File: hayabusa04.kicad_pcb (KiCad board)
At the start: 2 copper layers, 81.8 x 38.1 mm, 20 parts, among them SW1 SW_Push, SW2 MX_SW_HS, SW3 MX_SW_HS, SW4 MX_SW_HS, SW5 MX_SW_HS, U1 ATmega32U4-AU, Y1 16MHz

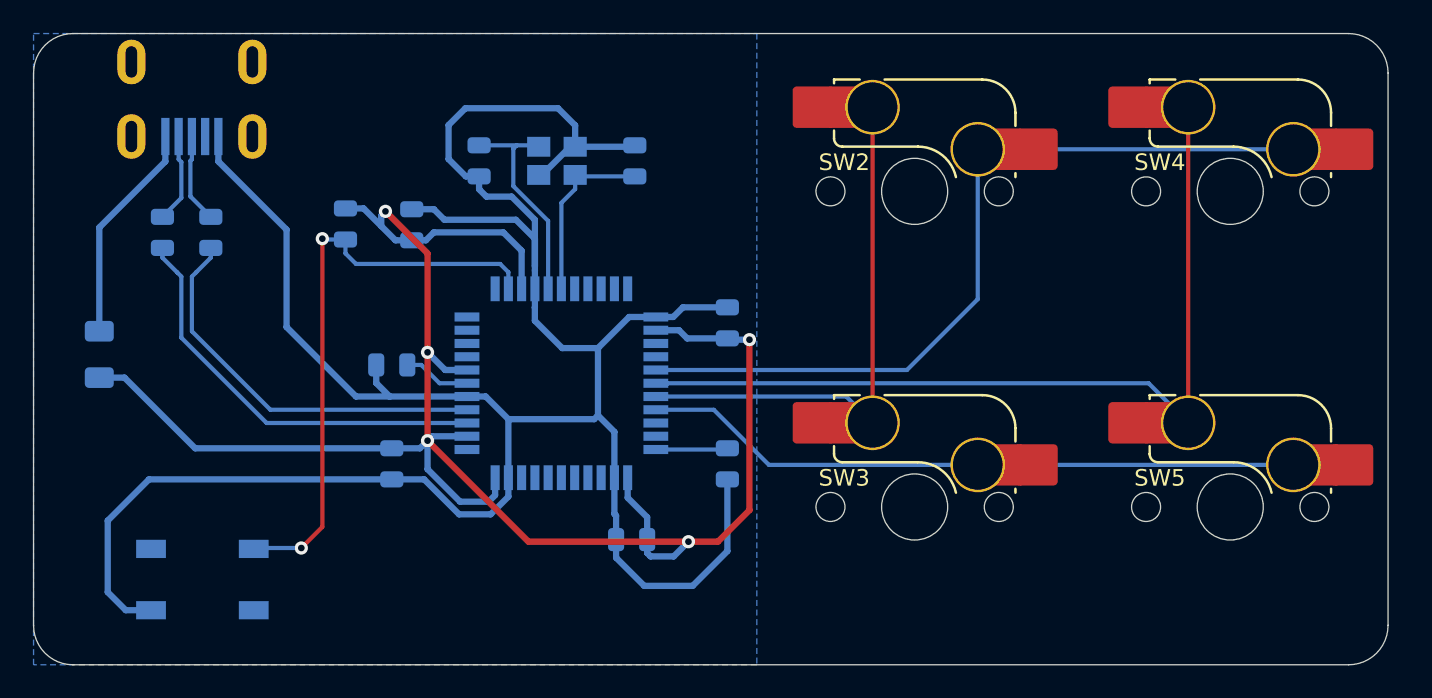
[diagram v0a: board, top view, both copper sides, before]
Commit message: routed usb c
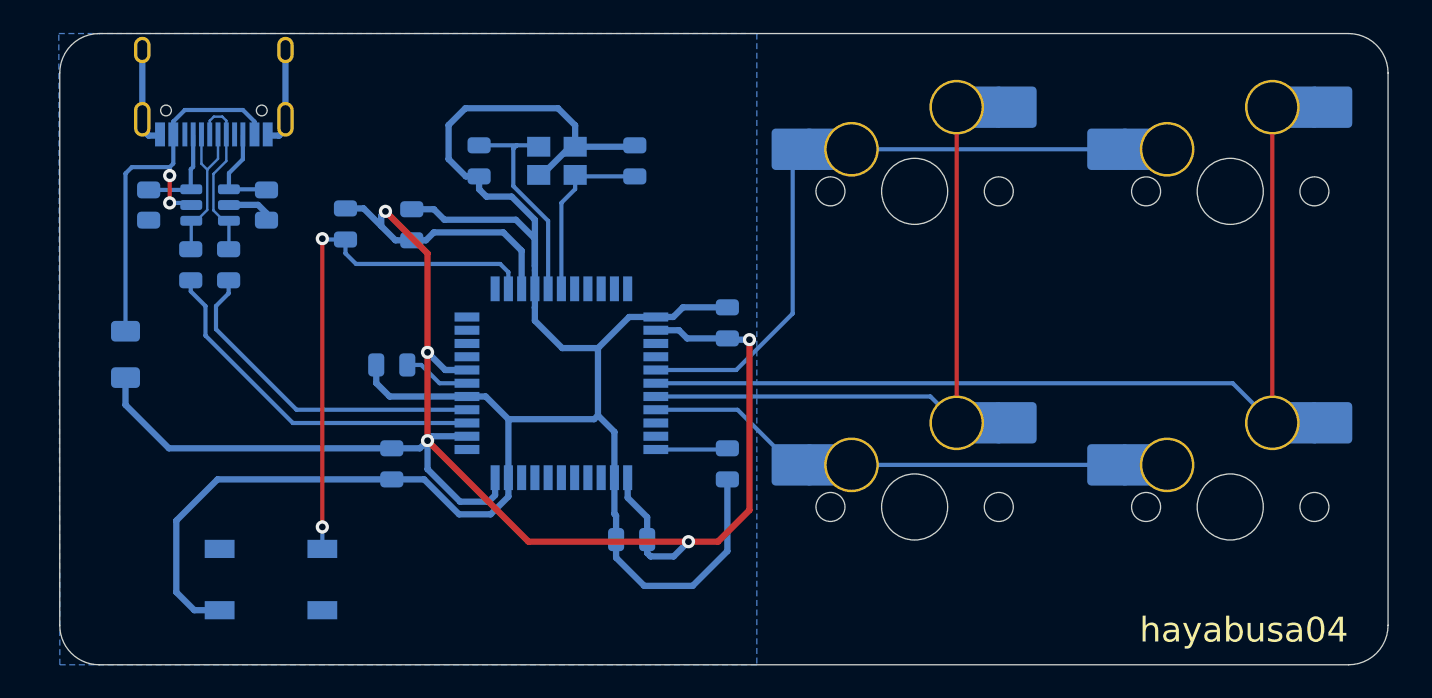
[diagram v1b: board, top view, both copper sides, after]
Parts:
- removed USB1: Molex-0548190589, random-keyboard-parts:Molex-0548190589
- added J1: USB_C_Receptacle_USB2.0, Connector_USB:USB_C_Receptacle_HRO_TYPE-C-31-M-12, B.Cu at (121.2, 57.6)
- added R5: 5.1k, Resistor_SMD:R_0805_2012Metric, B.Cu at (117.3, 65.9)
- added R6: 5.1k, Resistor_SMD:R_0805_2012Metric, B.Cu at (124.4, 65.9)
- added U2: SRV05-4, Package_TO_SOT_SMD:SOT-23-6, B.Cu at (121.0, 65.9)
- SW2, SW3, SW4, SW5: moved to B.Cu
- moved SW1 4.14 mm to (124.7, 88.5)
- moved R1 2.60 mm to (119.8, 69.5)
- moved R2 2.23 mm to (122.1, 69.5)
- moved F1 1.58 mm to (115.9, 74.9), turned to -90 degrees
- turned SW2 to 180 degrees
- turned SW3 to 180 degrees
- turned SW4 to 180 degrees
- turned SW5 to 180 degrees
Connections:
- F1 pad 1: +5V -> ESD5V
- F1 pad 2: VCC -> +5V
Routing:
- net ESD5V: track 0.00 -> 25.0 mm, vias 0 -> 2
- net ROW0: track 52.8 -> 38.6 mm
- net VCC: track 13.4 -> 0.00 mm
- net ROW1: track 39.9 -> 28.7 mm
- net GND: track 155.7 -> 145.3 mm
- net CC1: track 0.00 -> 5.92 mm
- net CC2: track 0.00 -> 5.89 mm
- net D+: track 5.40 -> 10.7 mm
- net COL0: track 32.8 -> 37.9 mm
- net D-: track 5.39 -> 9.96 mm
- net COL1: track 52.9 -> 57.2 mm
- net Net-(R2-Pad2): track 24.1 -> 20.4 mm
- net Net-(R1-Pad1): track 25.3 -> 21.7 mm
- net Net-(R3-Pad2): track 35.6 -> 32.3 mm
- net +5V: track 112.1 -> 111.5 mm
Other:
- board size 81.8 x 38.1 mm -> 80.2 x 38.1 mm
- board text added: "hayabusa04"

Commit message: generated gerber files
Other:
- rule pad_to_mask_clearance: 0.051 -> 0
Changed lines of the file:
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@@
   )
   (setup
-    (pad_to_mask_clearance 0.051)
-    (solder_mask_min_width 0.25)
+    (stackup
+      (layer "F.SilkS" (type "Top Silk Screen"))
+      (layer "F.Paste" (type "Top Solder Paste"))
+      (layer "F.Mask" (type "Top Solder Mask") (thickness 0.01))
+      (layer "F.Cu" (type "copper") (thickness 0.035))
+      (layer "dielectric 1" (type "core") (thickness 1.51) (material "FR4") (epsilon_r 4.5) (loss_tangent 0.02))
+      (layer "B.Cu" (type "copper") (thickness 0.035))
+      (layer "B.Mask" (type "Bottom Solder Mask") (thickness 0.01))
+      (layer "B.Paste" (type "Bottom Solder Paste"))
+      (layer "B.SilkS" (type "Bottom Silk Screen"))
+      (copper_finish "None")
+      (dielectric_constraints no)
+    )
+    (pad_to_mask_clearance 0)
     (pcbplotparams
-      (layerselection 0x00010fc_ffffffff)
+      (layerselection 0x00010f0_ffffffff)
       (disableapertmacros false)
-      (usegerberextensions false)
+      (usegerberextensions true)
       (usegerberattributes false)
       (usegerberadvancedattributes false)
@@
       (plotinvisibletext false)
       (sketchpadsonfab false)
-      (subtractmaskfromsilk false)
+      (subtractmaskfromsilk true)
       (outputformat 1)
       (mirror false)
-      (drillshape 1)
+      (drillshape 0)
       (scaleselection 1)
-      (outputdirectory "")
+      (outputdirectory "gerber/")
     )
   )
@@
     (fp_arc (start -4.864824 3.20022) (mid -4.718377 2.846667) (end -4.364824 2.70022) (layer "B.SilkS") (width 0.15))
     (fp_arc (start 2.494322 0.86022) (mid 1.670693 2.183637) (end 0.2 2.70022) (layer "B.SilkS") (width 0.15))
-    (fp_arc (start 6.085176 4.75022) (mid 5.499393 6.164439) (end 4.085176 6.75022) (layer "B.SilkS") (width 0.15))
+    (fp_arc (start 6.085176 4.75022) (mid 5.499394 6.164438) (end 4.085176 6.75022) (layer "B.SilkS") (width 0.15))
     (fp_line (start 9.525 9.525) (end 9.525 -9.525) (layer "Dwgs.User") (width 0.12))
     (fp_line (start 9.525 -9.525) (end -9.525 -9.525) (layer "Dwgs.User") (width 0.12))
@@
     (fp_line (start 8.685176 3.75022) (end 8.685176 1.30022) (layer "B.CrtYd") (width 0.05))
     (fp_arc (start 2.494322 0.86022) (mid 1.670502 2.183399) (end 0.2 2.70022) (layer "B.CrtYd") (width 0.05))
-    (fp_arc (start 6.085176 4.75022) (mid 5.499393 6.164439) (end 4.085176 6.75022) (layer "B.CrtYd") (width 0.05))
+    (fp_arc (start 6.085176 4.75022) (mid 5.499394 6.164438) (end 4.085176 6.75022) (layer "B.CrtYd") (width 0.05))
     (fp_line (start 7 7) (end 7 -7) (layer "F.CrtYd") (width 0.05))
     (fp_line (start -7 -7) (end -7 7) (layer "F.CrtYd") (width 0.05))
@@
     (fp_line (start -4.864824 6.75022) (end -4.864824 6.52022) (layer "B.SilkS") (width 0.15))
     (fp_line (start 4.085176 6.75022) (end -1.814824 6.75022) (layer "B.SilkS") (width 0.15))
-    (fp_arc (start 6.085176 4.75022) (mid 5.499393 6.164439) (end 4.085176 6.75022) (layer "B.SilkS") (width 0.15))
+    (fp_arc (start 6.085176 4.75022) (mid 5.499394 6.164438) (end 4.085176 6.75022) (layer "B.SilkS") (width 0.15))
     (fp_arc (start -4.864824 3.20022) (mid -4.718377 2.846667) (end -4.364824 2.70022) (layer "B.SilkS") (width 0.15))
     (fp_arc (start 2.494322 0.86022) (mid 1.670693 2.183637) (end 0.2 2.70022) (layer "B.SilkS") (width 0.15))
@@
     (fp_line (start 6.085176 3.75022) (end 8.685176 3.75022) (layer "B.CrtYd") (width 0.05))
     (fp_line (start -4.864824 2.70022) (end 0.2 2.70022) (layer "B.CrtYd") (width 0.05))
-    (fp_arc (start 6.085176 4.75022) (mid 5.499393 6.164439) (end 4.085176 6.75022) (layer "B.CrtYd") (width 0.05))
+    (fp_arc (start 6.085176 4.75022) (mid 5.499394 6.164438) (end 4.085176 6.75022) (layer "B.CrtYd") (width 0.05))
     (fp_arc (start 2.494322 0.86022) (mid 1.670502 2.183399) (end 0.2 2.70022) (layer "B.CrtYd") (width 0.05))
     (fp_line (start 7 7) (end 7 -7) (layer "F.CrtYd") (width 0.05))
@@
     (fp_line (start -1 -0.625) (end -1 0.625) (layer "B.Fab") (width 0.1))
     (fp_line (start -1 0.625) (end 1 0.625) (layer "B.Fab") (width 0.1))
-    (pad "1" smd roundrect (at -0.9125 0 270) (size 1.025 1.4) (layers "B.Cu" "B.Paste" "B.Mask") (roundrect_rratio 0.243902)
+    (pad "1" smd roundrect (at -0.9125 0 270) (size 1.025 1.4) (layers "B.Cu" "B.Paste" "B.Mask") (roundrect_rratio 0.243902439)
       (net 42 "CC2") (pintype "passive"))
-    (pad "2" smd roundrect (at 0.9125 0 270) (size 1.025 1.4) (layers "B.Cu" "B.Paste" "B.Mask") (roundrect_rratio 0.243902)
+    (pad "2" smd roundrect (at 0.9125 0 270) (size 1.025 1.4) (layers "B.Cu" "B.Paste" "B.Mask") (roundrect_rratio 0.243902439)
       (net 1 "GND") (pintype "passive"))
     (model "${KICAD6_3DMODEL_DIR}/Resistor_SMD.3dshapes/R_0805_2012Metric.wrl"
@@
     (fp_arc (start 2.494322 0.86022) (mid 1.670693 2.183637) (end 0.2 2.70022) (layer "B.SilkS") (width 0.15))
     (fp_arc (start -4.864824 3.20022) (mid -4.718377 2.846667) (end -4.364824 2.70022) (layer "B.SilkS") (width 0.15))
-    (fp_arc (start 6.085176 4.75022) (mid 5.499393 6.164439) (end 4.085176 6.75022) (layer "B.SilkS") (width 0.15))
+    (fp_arc (start 6.085176 4.75022) (mid 5.499394 6.164438) (end 4.085176 6.75022) (layer "B.SilkS") (width 0.15))
     (fp_line (start -9.525 -9.525) (end -9.525 9.525) (layer "Dwgs.User") (width 0.12))
     (fp_line (start -9.525 9.525) (end 9.525 9.525) (layer "Dwgs.User") (width 0.12))
@@
     (fp_line (start -7.414824 3.87022) (end -7.414824 6.32022) (layer "B.CrtYd") (width 0.05))
     (fp_line (start -4.864824 3.87022) (end -7.414824 3.87022) (layer "B.CrtYd") (width 0.05))
-    (fp_arc (start 6.085176 4.75022) (mid 5.499393 6.164439) (end 4.085176 6.75022) (layer "B.CrtYd") (width 0.05))
+    (fp_arc (start 6.085176 4.75022) (mid 5.499394 6.164438) (end 4.085176 6.75022) (layer "B.CrtYd") (width 0.05))
     (fp_arc (start 2.494322 0.86022) (mid 1.670502 2.183399) (end 0.2 2.70022) (layer "B.CrtYd") (width 0.05))
     (fp_line (start -7 -7) (end -7 7) (layer "F.CrtYd") (width 0.05))
@@
     (fp_line (start -1 -0.625) (end -1 0.625) (layer "B.Fab") (width 0.1))
     (fp_line (start -1 0.625) (end 1 0.625) (layer "B.Fab") (width 0.1))
-    (pad "1" smd roundrect (at -0.9125 0 90) (size 1.025 1.4) (layers "B.Cu" "B.Paste" "B.Mask") (roundrect_rratio 0.243902)
+    (pad "1" smd roundrect (at -0.9125 0 90) (size 1.025 1.4) (layers "B.Cu" "B.Paste" "B.Mask") (roundrect_rratio 0.243902439)
       (net 1 "GND") (pintype "passive"))
-    (pad "2" smd roundrect (at 0.9125 0 90) (size 1.025 1.4) (layers "B.Cu" "B.Paste" "B.Mask") (roundrect_rratio 0.243902)
+    (pad "2" smd roundrect (at 0.9125 0 90) (size 1.025 1.4) (layers "B.Cu" "B.Paste" "B.Mask") (roundrect_rratio 0.243902439)
       (net 41 "CC1") (pintype "passive"))
     (model "${KICAD6_3DMODEL_DIR}/Resistor_SMD.3dshapes/R_0805_2012Metric.wrl"
@@
     (fp_line (start -4.864824 6.75022) (end -4.864824 6.52022) (layer "B.SilkS") (width 0.15))
     (fp_arc (start -4.864824 3.20022) (mid -4.718377 2.846667) (end -4.364824 2.70022) (layer "B.SilkS") (width 0.15))
-    (fp_arc (start 6.085176 4.75022) (mid 5.499393 6.164439) (end 4.085176 6.75022) (layer "B.SilkS") (width 0.15))
+    (fp_arc (start 6.085176 4.75022) (mid 5.499394 6.164438) (end 4.085176 6.75022) (layer "B.SilkS") (width 0.15))
     (fp_arc (start 2.494322 0.86022) (mid 1.670693 2.183637) (end 0.2 2.70022) (layer "B.SilkS") (width 0.15))
     (fp_line (start -9.525 9.525) (end 9.525 9.525) (layer "Dwgs.User") (width 0.12))
@@
     (fp_line (start 6.085176 1.30022) (end 6.085176 0.86022) (layer "B.CrtYd") (width 0.05))
     (fp_arc (start 2.494322 0.86022) (mid 1.670502 2.183399) (end 0.2 2.70022) (layer "B.CrtYd") (width 0.05))
-    (fp_arc (start 6.085176 4.75022) (mid 5.499393 6.164439) (end 4.085176 6.75022) (layer "B.CrtYd") (width 0.05))
+    (fp_arc (start 6.085176 4.75022) (mid 5.499394 6.164438) (end 4.085176 6.75022) (layer "B.CrtYd") (width 0.05))
     (fp_line (start 7 -7) (end -7 -7) (layer "F.CrtYd") (width 0.05))
     (fp_line (start 7 7) (end 7 -7) (layer "F.CrtYd") (width 0.05))

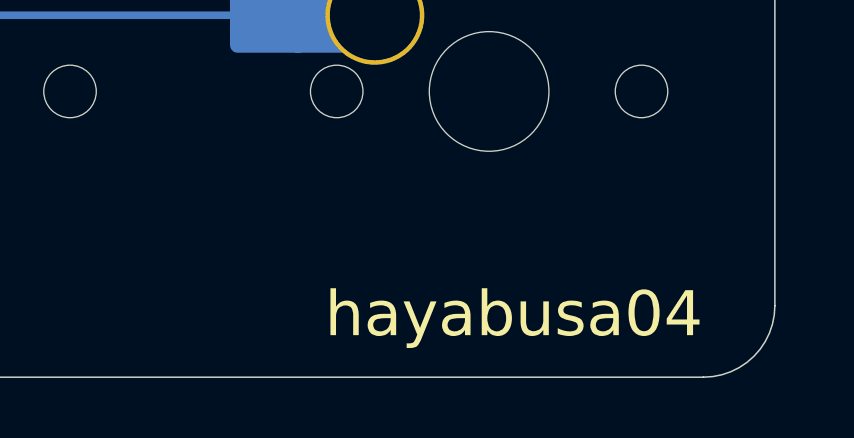
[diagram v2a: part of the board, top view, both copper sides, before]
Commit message: added 3d models
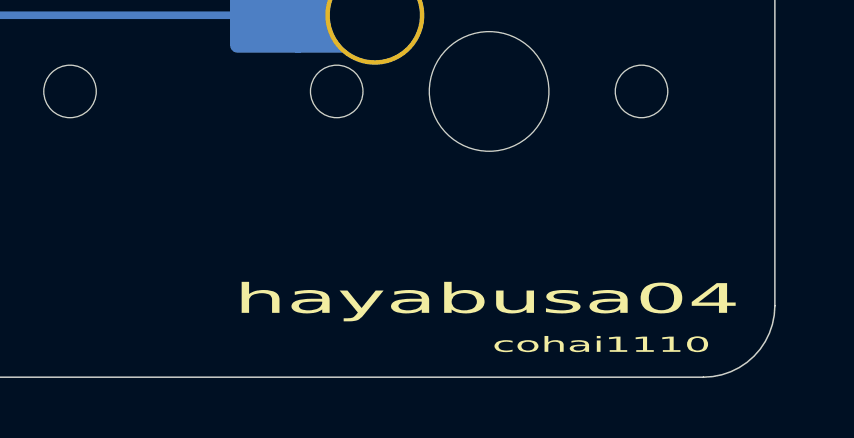
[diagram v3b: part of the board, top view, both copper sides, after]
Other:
- board text added: "cohai1110"
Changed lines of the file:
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@@
     (pad "3" smd rect locked (at 3.1 1.85 180) (size 1.8 1.1) (layers "B.Cu" "B.Paste" "B.Mask"))
     (pad "4" smd rect locked (at -3.1 -1.85 180) (size 1.8 1.1) (layers "B.Cu" "B.Paste" "B.Mask"))
-    (model "${KISYS3DMOD}/Button_Switch_SMD.3dshapes/SW_SPST_TL3342.step"
+    (model "${KICAD6_3DMODEL_DIR}/Button_Switch_SMD.3dshapes/SW_SPST_TL3342.step"
       (offset (xyz 0 0 0))
       (scale (xyz 1 1 1))
@@
       (rotate (xyz 180 0 0))
     )
+    (model "${KIPRJMOD}/marbastlib-mx.pretty/3d/HS_Kailh_MX.step"
+      (offset (xyz -4.826 6.7399916 1.905))
+      (scale (xyz 1 1 1))
+      (rotate (xyz 180 0 0))
+    )
   )
   (footprint "marbastlib-mx:SW_MX_HS_1u" (layer "B.Cu")
@@
       (rotate (xyz 180 0 0))
     )
+    (model "${KIPRJMOD}/marbastlib-mx.pretty/3d/HS_Kailh_MX.step"
+      (offset (xyz -4.826 6.7399916 1.905))
+      (scale (xyz 1 1 1))
+      (rotate (xyz 180 0 0))
+    )
   )
   (footprint "Resistor_SMD:R_0805_2012Metric" (layer "B.Cu")
@@
       (rotate (xyz 0 0 0))
     )
+    (model "${KIPRJMOD}/TYPE-C-31-M-12/TYPE-C-31-M-12.step"
+      (offset (xyz 0 -1.016 0))
+      (scale (xyz 1 1 1))
+      (rotate (xyz 90 180 180))
+    )
   )
   (footprint "marbastlib-mx:SW_MX_HS_1u" (layer "B.Cu")
@@
       (net 8 "COL0") (pinfunction "2") (pintype "passive"))
     (model "${KIPRJMOD}/marbastlib/3d/HS_Kailh_MX.step"
-      (offset (xyz -4.82 6.74 1.82))
+      (offset (xyz -0 6.7399916 1.8200116))
       (scale (xyz 1 1 1))
       (rotate (xyz 180 0 0))
@@
     (model "${KIPRJMOD}/../3d/HS_Kailh_MX.step"
       (offset (xyz -4.82 6.74 1.82))
+      (scale (xyz 1 1 1))
+      (rotate (xyz 180 0 0))
+    )
+    (model "${KIPRJMOD}/marbastlib-mx.pretty/3d/HS_Kailh_MX.step"
+      (offset (xyz -4.826 6.74624 1.905))
       (scale (xyz 1 1 1))
       (rotate (xyz 180 0 0))
@@
       (rotate (xyz 180 0 0))
     )
+    (model "${KIPRJMOD}/marbastlib-mx.pretty/3d/HS_Kailh_MX.step"
+      (offset (xyz -4.826 6.7399916 1.905))
+      (scale (xyz 1 1 1))
+      (rotate (xyz 180 0 0))
+    )
   )
   (footprint "Fuse:Fuse_1206_3216Metric" (layer "B.Cu")
@@
   (gr_arc (start 114.294567 93.6625) (mid 112.610751 92.965051) (end 111.913317 91.28125) (layer "Edge.Cuts") (width 0.05))
   (gr_line (start 189.70625 93.6625) (end 114.294567 93.6625) (layer "Edge.Cuts") (width 0.05))
-  (gr_text "hayabusa04" (at 183.388 91.567) (layer "F.SilkS")
-    (effects (font (size 1.5 1.5) (thickness 0.3)))
+  (gr_text "cohai1110" (at 186.309 92.583) (layer "F.SilkS")
+    (effects (font (size 0.508 1.016) (thickness 0.0992)))
+  )
+  (gr_text "hayabusa04" (at 182.499 91.059) (layer "F.SilkS")
+    (effects (font (size 0.992 2.008) (thickness 0.20228)))
   )
   (segment (start 131.826 77.47) (end 136.4915 77.47) (width 0.381) (layer "B.Cu") (net 1))

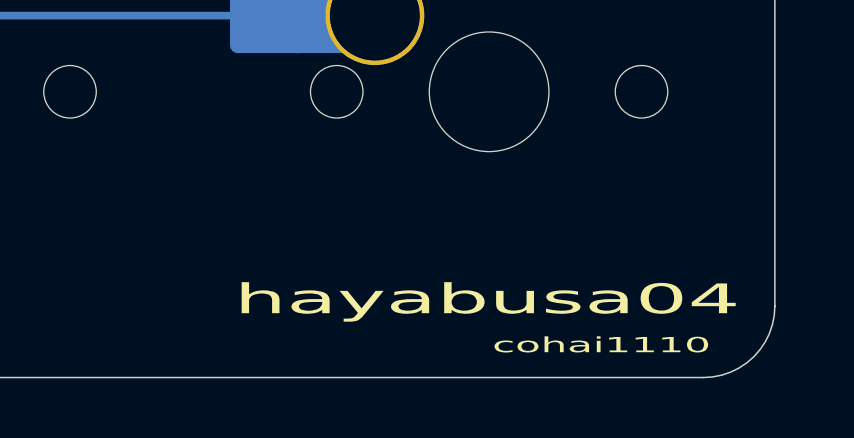
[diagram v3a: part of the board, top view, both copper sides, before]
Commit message: updated silk screen text
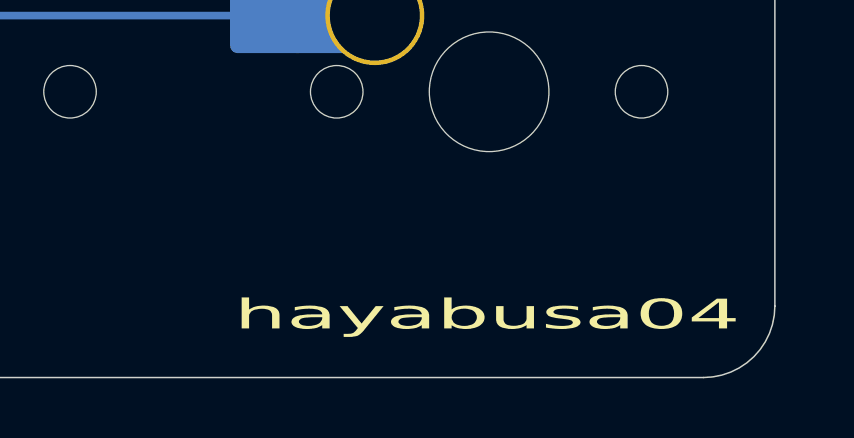
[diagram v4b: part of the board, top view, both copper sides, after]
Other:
- board text removed: "cohai1110"
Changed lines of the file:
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@@
   (gr_arc (start 114.294567 93.6625) (mid 112.610751 92.965051) (end 111.913317 91.28125) (layer "Edge.Cuts") (width 0.05))
   (gr_line (start 189.70625 93.6625) (end 114.294567 93.6625) (layer "Edge.Cuts") (width 0.05))
-  (gr_text "cohai1110" (at 186.309 92.583) (layer "F.SilkS")
-    (effects (font (size 0.508 1.016) (thickness 0.0992)))
-  )
-  (gr_text "hayabusa04" (at 182.499 91.059) (layer "F.SilkS")
+  (gr_text "hayabusa04" (at 182.499 91.567) (layer "F.SilkS")
     (effects (font (size 0.992 2.008) (thickness 0.20228)))
   )
